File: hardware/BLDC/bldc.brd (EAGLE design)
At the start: 51 x 40 mm, 83 parts, among them J1 PWR_2_XT30PW-M, J2 LINEAR_3_JST_PH_RA, J3 LINEAR_8_JST_PH_RA, U1 MA702, U10 MCP2542FD, U11 LDFM33PUR, U2 DRV8323RS, U3 TPN7R006PL, U4 TPN7R006PL, U5 TPN7R006PL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

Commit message: Prior to enlarging 24v plane
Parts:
- C1, C34, C35: value 1uf 10v -> 1uF 10V
- C13, C15, C2, C36, C4, C41, C43, C6, C7, C8: value 100nF 10V -> 0.1uF 10V
- C14: value 10uF 50V -> 10uF 25V
- C31, C32: value 1uf 50v -> 1uF 50V
- C33: value 47nF 50v -> 47nF 50V
- C37, C42: value 6.8pF 10V -> 10pF 10V
- J2: value LINEAR_3_JST_PH_RA -> LINEAR_35040500391; device _T_conn:JST_SM03B-SRSS-TB -> _T_conn:MOLEX_5040500391
- J3: value LINEAR_8_JST_PH_RA -> LINEAR_85040500891; device _T_conn:JST_SM08B-SRSS-TB -> _T_conn:MOLEX_5040500891
- R8, R9: value 10k -> 10k 1%
- moved J3 4.44 mm to (13.6, 33.6), turned to 0 degrees
- moved C6 2.91 mm to (22.8, 35.3)
- moved C9 2.91 mm to (24.4, 35.3)
- moved J2 2.37 mm to (44.6, 25.9), turned to 90 degrees
- moved J1 1.10 mm to (47.9, 14.7)
- moved C17 1.00 mm to (42.9, 13.6)
- moved C18 1.00 mm to (42.9, 15.7)
- moved C19 1.00 mm to (42.9, 17.8)
- moved C20 1.00 mm to (47.1, 17.8)
- moved C21 1.00 mm to (47.1, 15.7)
- moved C22 1.00 mm to (47.1, 13.6)
- moved C23 1.00 mm to (47.1, 11.5)
- moved C30 1.00 mm to (42.9, 11.5)
- moved D2 1.00 mm to (47.8, 24.6)
- moved D3 1.00 mm to (47.8, 25.9)
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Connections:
- net +3V3: now also J3.P1; no longer J3.1
- net GND: now also J2.P3, J3.P8; no longer J2.3, J3.8
- net LPUART1_RX: now also J3.P7; no longer J3.7
- net LPUART1_TX: now also J3.P6; no longer J3.6
- net N$11: now also J2.P1; no longer J2.1
- net N$12: now also J2.P2; no longer J2.2
- net NRST: now also J3.P2; no longer J3.2
- net SWCLK: now also J3.P3; no longer J3.3
- net SWDIO: now also J3.P4; no longer J3.4
- net SWO: now also J3.P5; no longer J3.5
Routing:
- net NRST: track 13.9 -> 19.1 mm, vias 0 -> 2
- net LPUART1_TX: track 18.0 -> 13.6 mm
- net SWCLK: track 23.1 -> 26.8 mm
- net SWO: track 23.4 -> 20.0 mm, vias 2 -> 0
- net +24V: track 42.0 -> 44.9 mm
- net SWDIO: track 25.7 -> 28.6 mm, vias 0 -> 2
- net GND: track 71.5 -> 69.0 mm, vias 125 -> 121
- net +3V3: track 46.2 -> 44.7 mm
- net N$12: track 8.84 -> 7.57 mm
- net LED3: track 32.6 -> 33.2 mm
- net LED2: track 31.1 -> 31.7 mm
- net LPUART1_RX: track 19.3 -> 18.7 mm

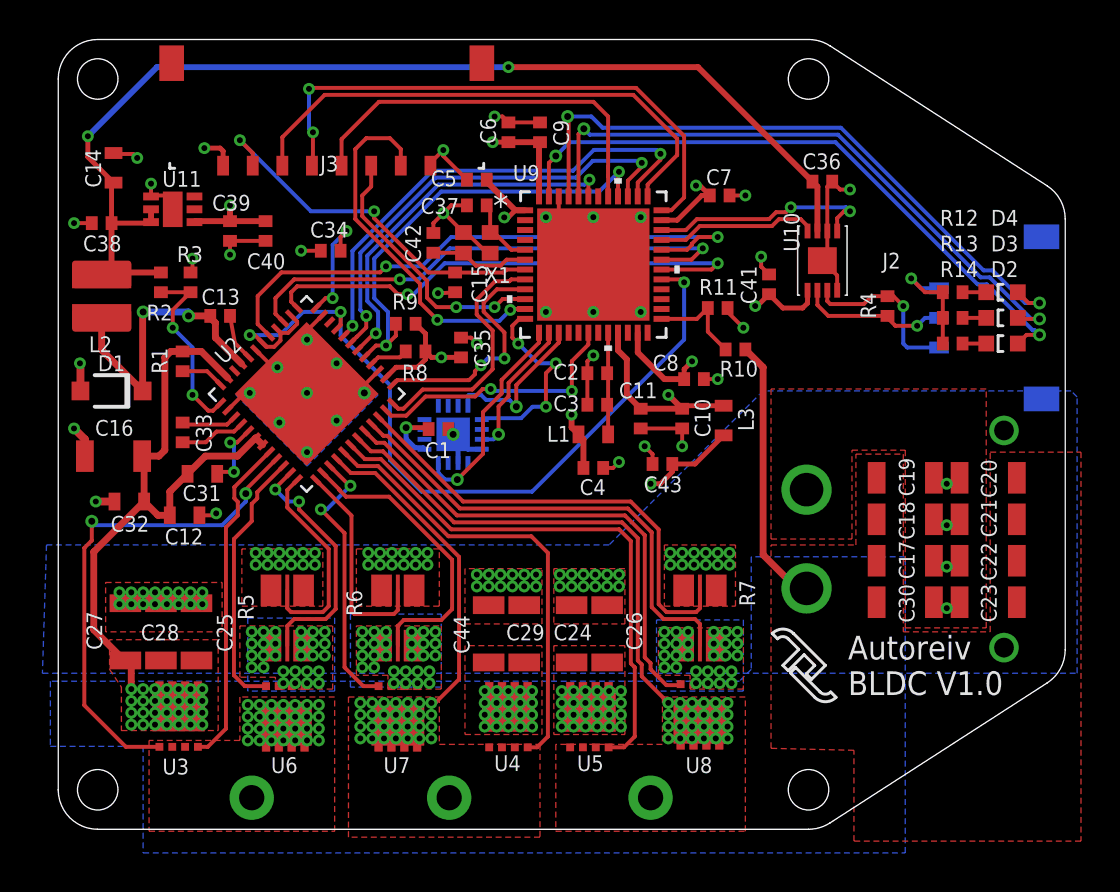
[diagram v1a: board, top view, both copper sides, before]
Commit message: Increased +24V plane size
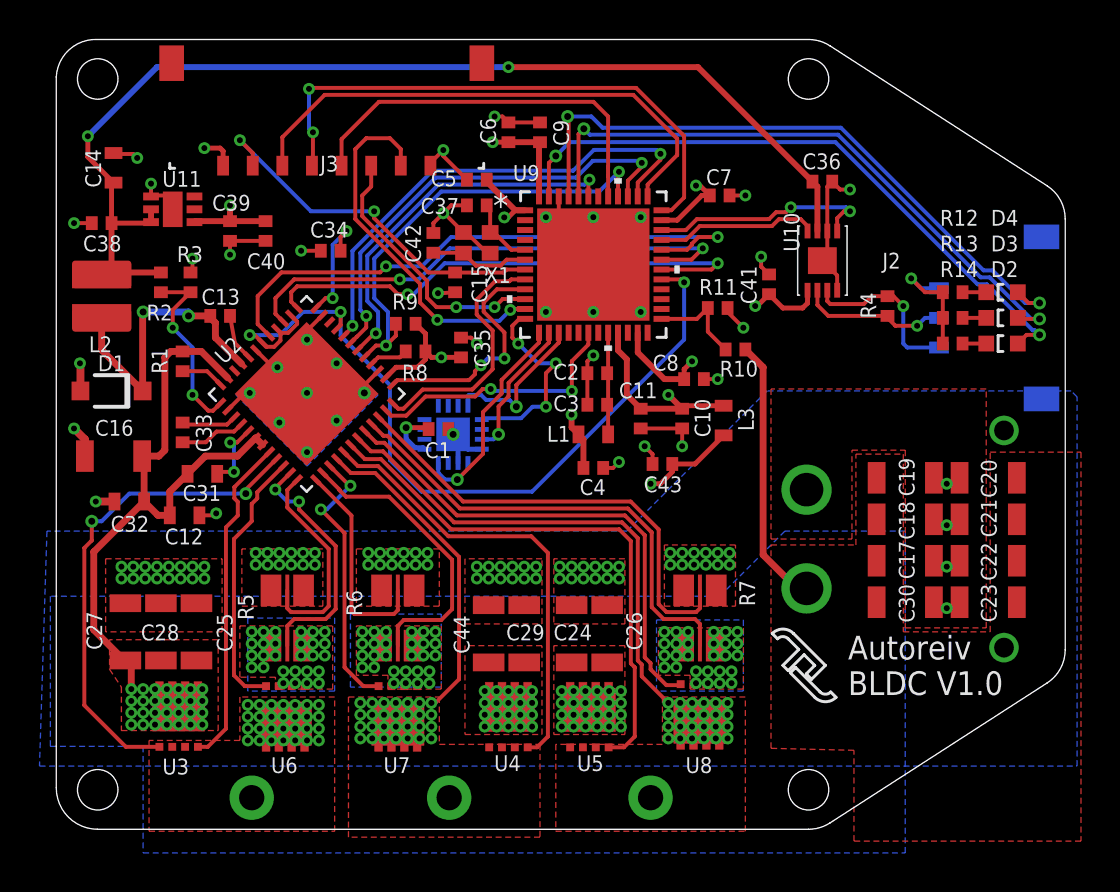
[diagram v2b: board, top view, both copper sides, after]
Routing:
- net SHA: track 25.7 -> 25.2 mm
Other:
- board size 51 x 40 mm -> 51.1 x 40 mm

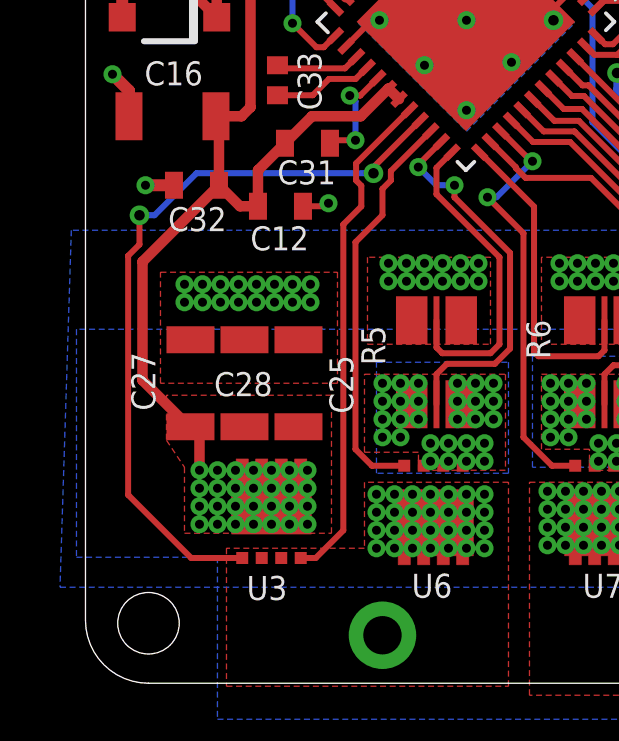
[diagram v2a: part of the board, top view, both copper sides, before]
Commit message: Separated 24V line from fet plane
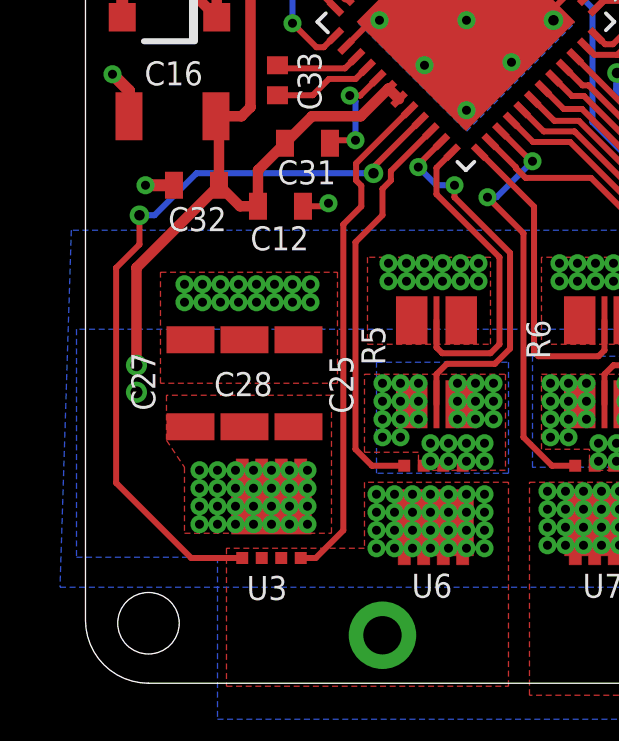
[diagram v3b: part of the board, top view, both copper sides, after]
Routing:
- net +24V: track 44.9 -> 41.6 mm, vias 72 -> 74
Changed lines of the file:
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@@
 </layers>
 <board>
-<fusionsync huburn="a.YnVzaW5lc3M6Z21haWwyMjE5MTc" projecturn="a.YnVzaW5lc3M6Z21haWwyMjE5MTcjMjAxOTA2MjkyMDE0MTU5NzY" f3durn="urn:adsk.wipprod:dm.lineage:e4urj2y-ReajaBtUk_DaUw" pcbguid="" lastpulledtime="" lastsyncedchangeguid="" latestrevisionid="cccc2e93-2fd3-40de-9739-6985b2d5cef6" lastsyncedrevisionid="cccc2e93-2fd3-40de-9739-6985b2d5cef6" lastboardhashguid="7721e2d3-fc54-e313-3a0b-e8c6d3c06d97" lastpushedtime="2020-05-25T21:01:21Z" linktopcb3d="%12"/>
+<fusionsync huburn="a.YnVzaW5lc3M6Z21haWwyMjE5MTc" projecturn="a.YnVzaW5lc3M6Z21haWwyMjE5MTcjMjAxOTA2MjkyMDE0MTU5NzY" f3durn="urn:adsk.wipprod:dm.lineage:e4urj2y-ReajaBtUk_DaUw" pcbguid="" lastpulledtime="" lastsyncedchangeguid="" latestrevisionid="8069666b-c29d-40c8-95b8-77e12e630a56" lastsyncedrevisionid="8069666b-c29d-40c8-95b8-77e12e630a56" lastboardhashguid="09fbb900-a4dd-8110-e375-94f34319935a" lastpushedtime="2020-05-25T21:31:11Z" linktopcb3d="%12"/>
 <plain>
 <wire x1="39.0836" y1="39.681" x2="38" y2="40" width="0" layer="20" curve="32.8049"/>
@@
 <wire x1="4.25" y1="18.9" x2="4.35" y2="18.8" width="0.35" layer="1"/>
 <wire x1="4.35" y1="18.8" x2="4.35" y2="16.6" width="0.35" layer="1"/>
-<wire x1="4.35" y1="16.6" x2="1.8" y2="14.05" width="0.35" layer="1"/>
-<wire x1="3.7" y1="8.2" x2="3.7" y2="7.1" width="0.35" layer="1"/>
-<wire x1="3.7" y1="8.2" x2="1.8" y2="10.1" width="0.35" layer="1"/>
-<wire x1="1.8" y1="14.05" x2="1.8" y2="10.1" width="0.35" layer="1"/>
+<wire x1="4.35" y1="16.6" x2="1.6" y2="13.85" width="0.35" layer="1"/>
+<wire x1="1.6" y1="13.85" x2="1.6" y2="10.6" width="0.35" layer="1"/>
 <wire x1="4.35" y1="16.6" x2="5.05" y2="15.9" width="0.35" layer="1"/>
 <wire x1="5.65" y1="15.9" x2="5.05" y2="15.9" width="0.35" layer="1"/>
@@
 <wire x1="5.4" y1="19.2" x2="5.1" y2="18.9" width="0.35" layer="1"/>
 <wire x1="5.1" y1="18.9" x2="4.25" y2="18.9" width="0.35" layer="1"/>
+<via x="1.6" y="10.6" extent="1-16" drill="0.4"/>
+<wire x1="1.6" y1="10.6" x2="1.6" y2="9.7" width="0.35" layer="2"/>
+<via x="1.6" y="9.7" extent="1-16" drill="0.4"/>
 </signal>
 <signal name="N$11">
@@
 <via x="1.7" y="15.6" extent="1-16" drill="0.35"/>
 <wire x1="1.7" y1="15.6" x2="1.7" y2="14.62628125" width="0.2" layer="1"/>
-<wire x1="1.7" y1="14.62628125" x2="1.3218" y2="14.24808125" width="0.2" layer="1"/>
+<wire x1="1.7" y1="14.62628125" x2="0.9218" y2="13.84808125" width="0.2" layer="1"/>
 <wire x1="3.425" y1="4.175" x2="5.125" y2="4.175" width="0.2" layer="1"/>
-<wire x1="1.3218" y1="14.24808125" x2="1.3218" y2="6.2782" width="0.2" layer="1"/>
-<wire x1="1.3218" y1="6.2782" x2="3.425" y2="4.175" width="0.2" layer="1"/>
+<wire x1="0.9218" y1="13.84808125" x2="0.9218" y2="6.6782" width="0.2" layer="1"/>
+<wire x1="0.9218" y1="6.6782" x2="3.425" y2="4.175" width="0.2" layer="1"/>
 <wire x1="9.5" y1="17" x2="3.6" y2="17" width="0.2" layer="16"/>
 <wire x1="2.2" y1="15.6" x2="1.7" y2="15.6" width="0.2" layer="16"/>

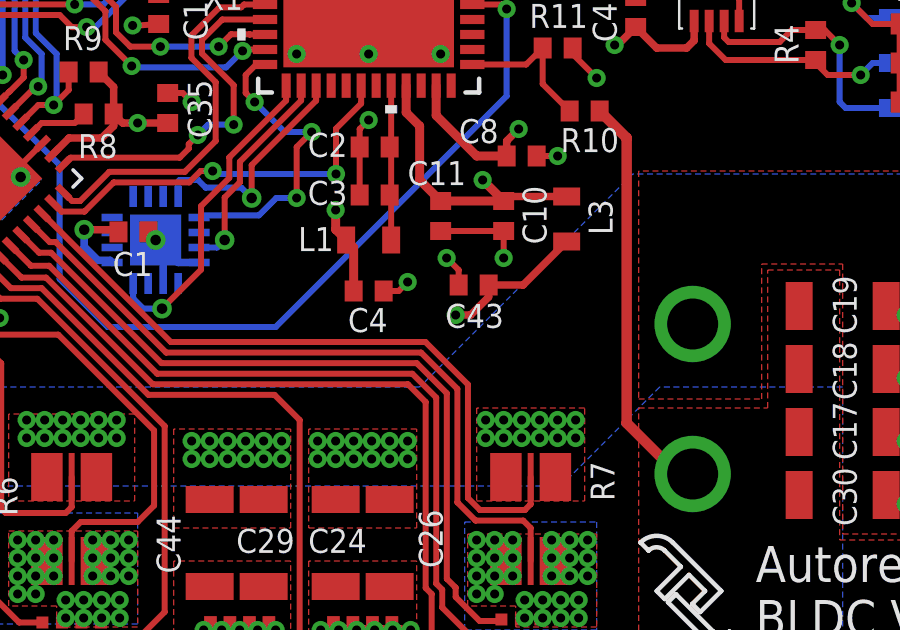
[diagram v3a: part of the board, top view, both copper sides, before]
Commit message: Pushed a 3.3v slightly more into power plane
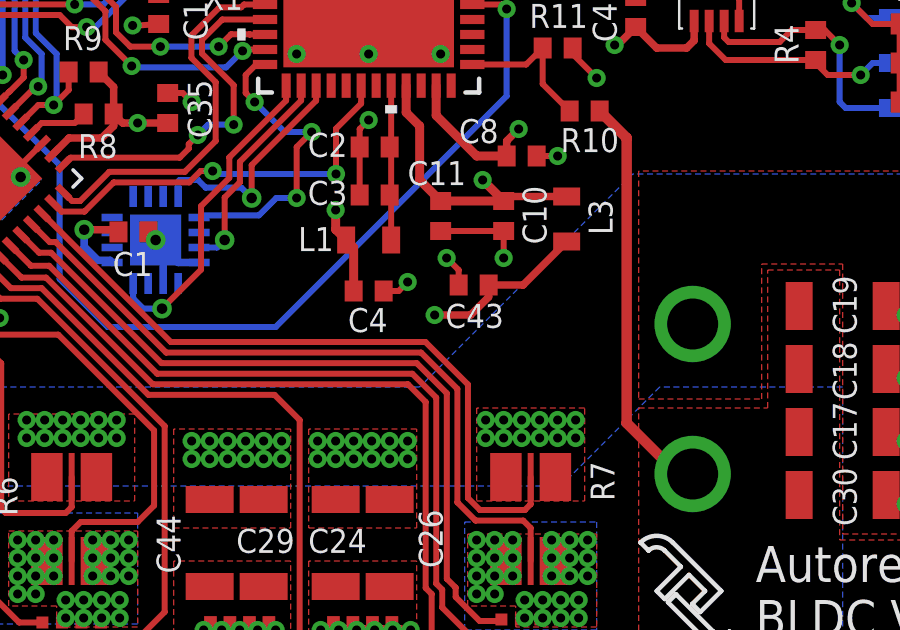
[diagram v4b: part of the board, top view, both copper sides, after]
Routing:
- net +3V3: track 44.7 -> 45.4 mm
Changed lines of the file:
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@@
 <wire x1="31.1" y1="18.5" x2="31.1" y2="18.1" width="0.25" layer="1"/>
 <wire x1="31.1" y1="18.1" x2="30.5" y2="17.5" width="0.25" layer="1"/>
-<wire x1="30.5" y1="17.5" x2="30" y2="17.5" width="0.25" layer="1"/>
-<via x="30" y="17.5" extent="1-16" drill="0.3"/>
+<wire x1="30.5" y1="17.5" x2="29.3" y2="17.5" width="0.25" layer="1"/>
+<via x="29.3" y="17.5" extent="1-16" drill="0.3"/>
 <wire x1="23.15" y1="31.35" x2="22.789553125" y2="30.989553125" width="0.25" layer="1"/>
 <wire x1="22.589553125" y1="30.989553125" x2="22.789553125" y2="30.989553125" width="0.25" layer="1"/>

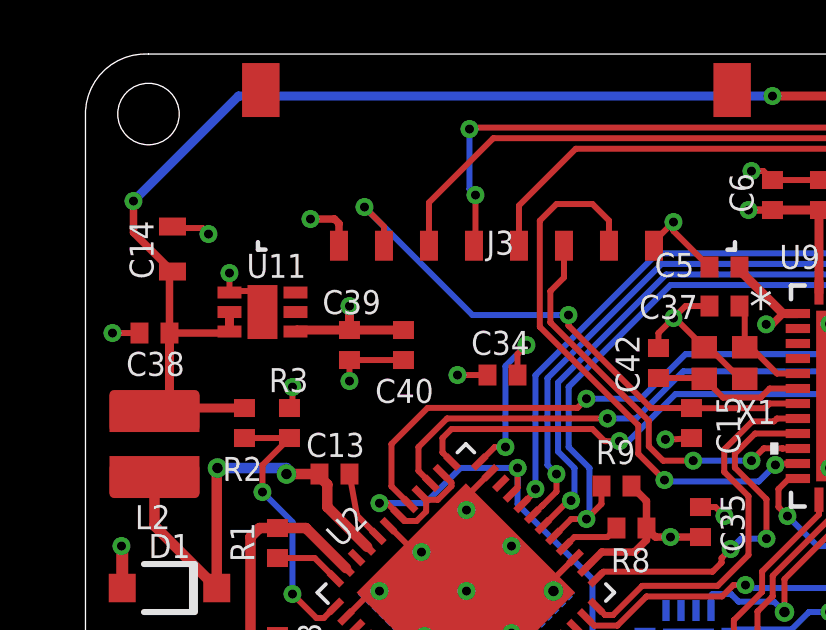
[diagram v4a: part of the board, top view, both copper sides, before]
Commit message: Increased connection with 3.3v plane
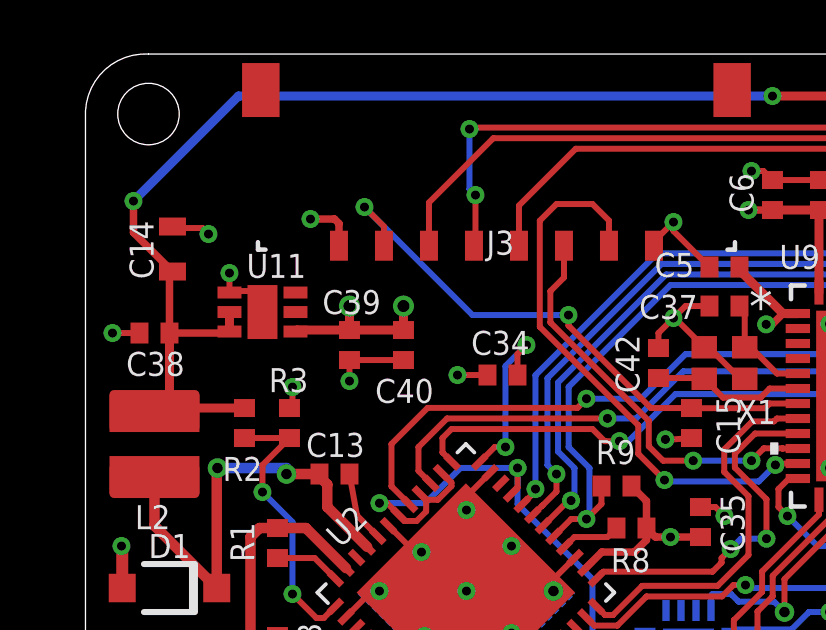
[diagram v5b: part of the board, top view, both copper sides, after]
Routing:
- net +3V3: track 45.4 -> 46.2 mm, vias 11 -> 12
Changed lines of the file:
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@@
 </layers>
 <board>
-<fusionsync huburn="a.YnVzaW5lc3M6Z21haWwyMjE5MTc" projecturn="a.YnVzaW5lc3M6Z21haWwyMjE5MTcjMjAxOTA2MjkyMDE0MTU5NzY" f3durn="urn:adsk.wipprod:dm.lineage:e4urj2y-ReajaBtUk_DaUw" pcbguid="" lastpulledtime="" lastsyncedchangeguid="" latestrevisionid="8069666b-c29d-40c8-95b8-77e12e630a56" lastsyncedrevisionid="8069666b-c29d-40c8-95b8-77e12e630a56" lastboardhashguid="09fbb900-a4dd-8110-e375-94f34319935a" lastpushedtime="2020-05-25T21:31:11Z" linktopcb3d="%12"/>
+<fusionsync huburn="a.YnVzaW5lc3M6Z21haWwyMjE5MTc" projecturn="a.YnVzaW5lc3M6Z21haWwyMjE5MTcjMjAxOTA2MjkyMDE0MTU5NzY" f3durn="urn:adsk.wipprod:dm.lineage:e4urj2y-ReajaBtUk_DaUw" pcbguid="" lastpulledtime="" lastsyncedchangeguid="" latestrevisionid="5ab0fcfe-19a7-49a8-88f9-f48e4d51edb4" lastsyncedrevisionid="5ab0fcfe-19a7-49a8-88f9-f48e4d51edb4" lastboardhashguid="fa3fa4ad-24f9-762d-9a10-17342891fb0a" lastpushedtime="2020-05-25T21:32:26Z" linktopcb3d="%12"/>
 <plain>
 <wire x1="39.0836" y1="39.681" x2="38" y2="40" width="0" layer="20" curve="32.8049"/>
@@
 <wire x1="8.7" y1="30.8" x2="10.5" y2="30.8" width="0.3" layer="1"/>
 <wire x1="8.7" y1="30.8" x2="8.7" y2="31.6" width="0.3" layer="1"/>
-<via x="8.7" y="31.6" extent="1-16" drill="0.3"/>
+<via x="8.7" y="31.6" extent="1-16" drill="0.4"/>
 <via x="19.4" y="23.9" extent="1-16" drill="0.3"/>
 <wire x1="23.6456" y1="31.35" x2="23.15" y2="31.35" width="0.3" layer="1"/>
@@
 <wire x1="8.35" y1="34.35" x2="8.2" y2="34.5" width="0.25" layer="1"/>
 <wire x1="8.2" y1="34.5" x2="7.4" y2="34.5" width="0.25" layer="1"/>
+<wire x1="10.5" y1="30.8" x2="10.5" y2="31.6" width="0.3" layer="1"/>
+<via x="10.5" y="31.6" extent="1-16" drill="0.4"/>
 </signal>
 <signal name="N$1">

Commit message: Sent to PCBWAY
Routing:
- net +24V: track 41.6 -> 42.3 mm
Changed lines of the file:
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@@
 </layers>
 <board>
-<fusionsync huburn="a.YnVzaW5lc3M6Z21haWwyMjE5MTc" projecturn="a.YnVzaW5lc3M6Z21haWwyMjE5MTcjMjAxOTA2MjkyMDE0MTU5NzY" f3durn="urn:adsk.wipprod:dm.lineage:e4urj2y-ReajaBtUk_DaUw" pcbguid="" lastpulledtime="" lastsyncedchangeguid="" latestrevisionid="5ab0fcfe-19a7-49a8-88f9-f48e4d51edb4" lastsyncedrevisionid="5ab0fcfe-19a7-49a8-88f9-f48e4d51edb4" lastboardhashguid="fa3fa4ad-24f9-762d-9a10-17342891fb0a" lastpushedtime="2020-05-25T21:32:26Z" linktopcb3d="%12"/>
+<fusionsync huburn="a.YnVzaW5lc3M6Z21haWwyMjE5MTc" projecturn="a.YnVzaW5lc3M6Z21haWwyMjE5MTcjMjAxOTA2MjkyMDE0MTU5NzY" f3durn="urn:adsk.wipprod:dm.lineage:e4urj2y-ReajaBtUk_DaUw" pcbguid="" lastpulledtime="" lastsyncedchangeguid="" latestrevisionid="848c6747-3f4d-4eaa-9d78-3698b7bdd824" lastsyncedrevisionid="848c6747-3f4d-4eaa-9d78-3698b7bdd824" lastboardhashguid="77e990b0-cea2-1a33-f5c1-3a22372c9ebf" lastpushedtime="2020-05-25T21:34:19Z" linktopcb3d="%12"/>
 <plain>
 <wire x1="39.0836" y1="39.681" x2="38" y2="40" width="0" layer="20" curve="32.8049"/>
@@
 <contactref element="C2" pad="2"/>
 <contactref element="R11" pad="1"/>
-<polygon width="0.1524" layer="1" isolate="0.25" thermals="no" rank="2">
+<polygon width="0.1524" layer="1" isolate="0.5" thermals="no" rank="2">
 <vertex x="40.2" y="14.7"/>
 <vertex x="40.2" y="19.2"/>
@@
 <wire x1="4.25" y1="18.9" x2="4.35" y2="18.8" width="0.35" layer="1"/>
 <wire x1="4.35" y1="18.8" x2="4.35" y2="16.6" width="0.35" layer="1"/>
-<wire x1="4.35" y1="16.6" x2="1.6" y2="13.85" width="0.35" layer="1"/>
 <wire x1="1.6" y1="13.85" x2="1.6" y2="10.6" width="0.35" layer="1"/>
 <wire x1="4.35" y1="16.6" x2="5.05" y2="15.9" width="0.35" layer="1"/>
@@
 <wire x1="9.076446875" y1="18.9" x2="9.999059375" y2="19.8226125" width="0.35" layer="1"/>
 <wire x1="7.45" y1="18.9" x2="9.076446875" y2="18.9" width="0.35" layer="1"/>
-<wire x1="34.8" y1="24.3" x2="35.7" y2="23.4" width="0.35" layer="1"/>
-<wire x1="35.7" y1="13.9" x2="37" y2="12.6" width="0.35" layer="1"/>
-<wire x1="35.7" y1="23.4" x2="35.7" y2="13.9" width="0.35" layer="1"/>
+<wire x1="34.8" y1="14.8" x2="37" y2="12.6" width="0.35" layer="1"/>
+<wire x1="34.8" y1="24.3" x2="34.8" y2="14.8" width="0.35" layer="1"/>
 <contactref element="U2" pad="7"/>
 <wire x1="9.999059375" y1="19.8226125" x2="10.3526125" y2="19.469059375" width="0.35" layer="1"/>
@@
 <wire x1="1.6" y1="10.6" x2="1.6" y2="9.7" width="0.35" layer="2"/>
 <via x="1.6" y="9.7" extent="1-16" drill="0.4"/>
+<wire x1="4.35" y1="16.6" x2="4.1" y2="16.35" width="0.35" layer="1"/>
+<wire x1="4.1" y1="16.35" x2="4.1" y2="15.2" width="0.35" layer="1"/>
+<wire x1="4.1" y1="15.2" x2="3.7" y2="14.8" width="0.35" layer="1"/>
+<wire x1="2.55" y1="14.8" x2="1.6" y2="13.85" width="0.35" layer="1"/>
+<wire x1="3.7" y1="14.8" x2="2.55" y2="14.8" width="0.35" layer="1"/>
 </signal>
 <signal name="N$11">
@@
 <via x="9.5" y="17" extent="1-16" drill="0.35"/>
 <via x="1.7" y="15.6" extent="1-16" drill="0.35"/>
-<wire x1="1.7" y1="15.6" x2="1.7" y2="14.62628125" width="0.2" layer="1"/>
-<wire x1="1.7" y1="14.62628125" x2="0.9218" y2="13.84808125" width="0.2" layer="1"/>
+<wire x1="1.7" y1="15.6" x2="1.7" y2="15.52628125" width="0.2" layer="1"/>
+<wire x1="1.7" y1="15.52628125" x2="0.9218" y2="14.74808125" width="0.2" layer="1"/>
 <wire x1="3.425" y1="4.175" x2="5.125" y2="4.175" width="0.2" layer="1"/>
-<wire x1="0.9218" y1="13.84808125" x2="0.9218" y2="6.6782" width="0.2" layer="1"/>
+<wire x1="0.9218" y1="14.74808125" x2="0.9218" y2="6.6782" width="0.2" layer="1"/>
 <wire x1="0.9218" y1="6.6782" x2="3.425" y2="4.175" width="0.2" layer="1"/>
 <wire x1="9.5" y1="17" x2="3.6" y2="17" width="0.2" layer="16"/>
